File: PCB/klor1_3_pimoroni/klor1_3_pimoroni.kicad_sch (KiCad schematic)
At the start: 86 parts, among them J1 MJ-4PP-9, J2 Haptic Buzz, J3 lv27, SW1 SW_PUSH-MX_W_LED, SW10 SW_PUSH-MX_W_LED, SW11 SW_PUSH-MX_W_LED, SW12 SW_PUSH-MX_W_LED, SW13 SW_PUSH-MX_W_LED, SW14 SW_PUSH-MX_W_LED, SW15 SW_PUSH-MX_W_LED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

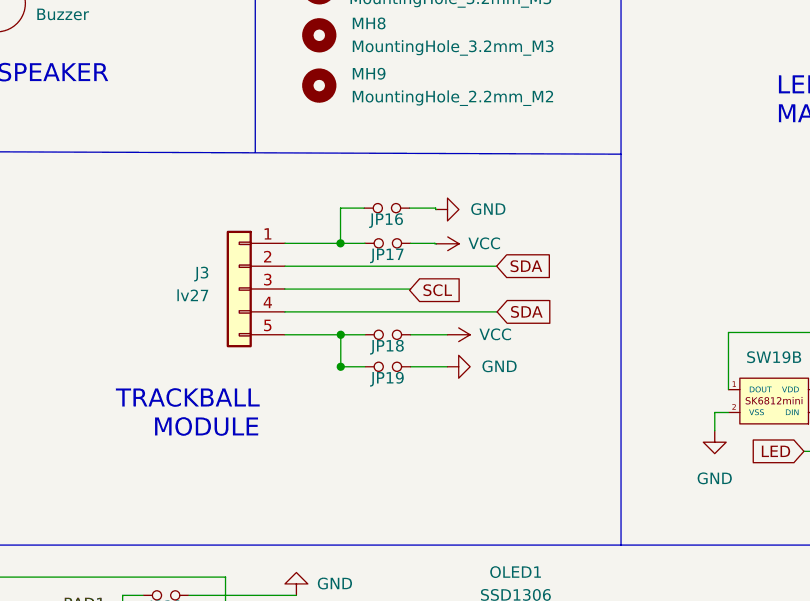
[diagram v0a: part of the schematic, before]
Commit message: Updated Gerbers
Got the JPs fixed to match wiring, that was a PITA.
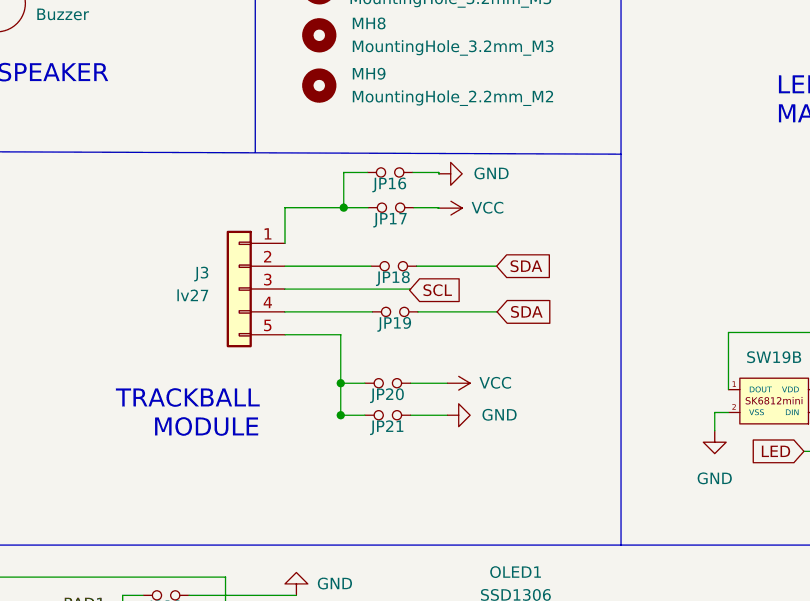
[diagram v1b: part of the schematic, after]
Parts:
- added JP18, JP19: Device_Jumper_NO_Small, KLOR:Jumper, symbol KLORlib:Device_Jumper_NO_Small
- renumbered JP18 to JP20, JP19 to JP21
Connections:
- net SDA: now also JP18.2, JP19.2; no longer J3.2 (Pin_2), J3.4 (Pin_4)
- new net: J3.2 (Pin_2), JP18.1
- new net: J3.4 (Pin_4), JP19.1
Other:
- moved on the sheet: JP16, JP17, JP20, JP21
